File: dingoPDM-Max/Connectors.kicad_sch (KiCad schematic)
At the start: 13 parts, among them J1 RedCubeTerminal, J2 USB_C_Receptacle_USB2.0, J3 RedCubeTerminal, J4 Conn_01x12

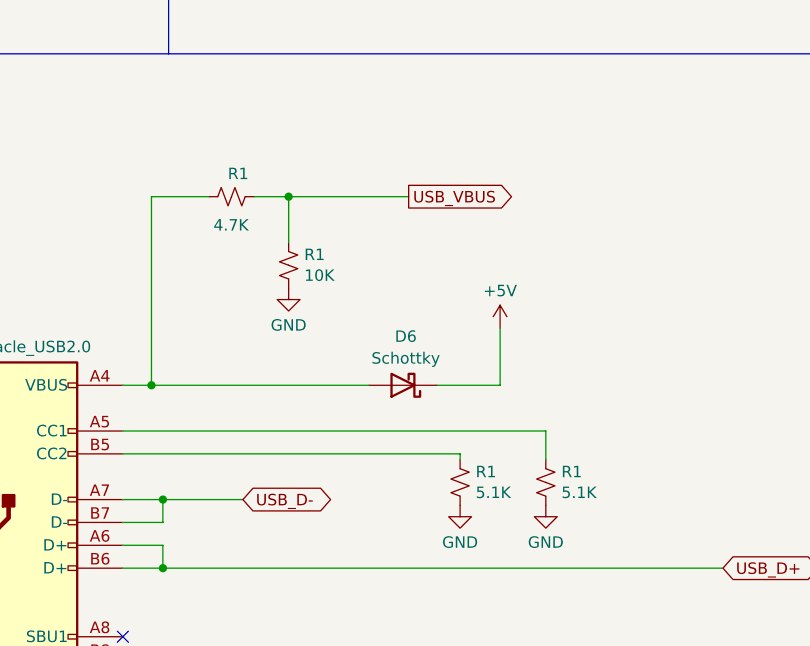
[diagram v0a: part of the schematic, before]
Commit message: Updated to Kicad 8
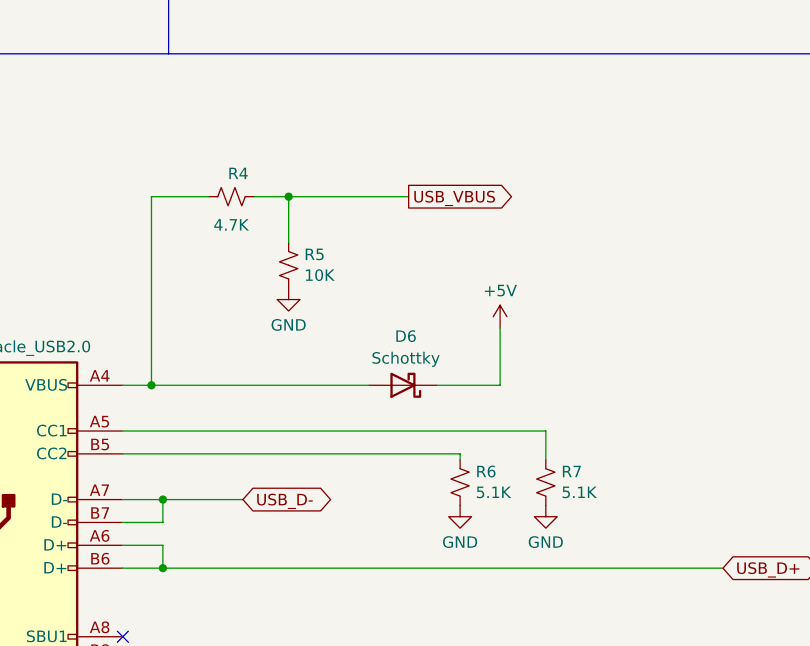
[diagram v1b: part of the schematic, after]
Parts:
- renumbered R1 to R4, R1 to R5, R1 to R6, R1 to R7

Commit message: add dc-dc options and 5v cap
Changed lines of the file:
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@@
 (kicad_sch
-	(version 20231120)
+	(version 20250114)
 	(generator "eeschema")
-	(generator_version "8.0")
+	(generator_version "9.0")
 	(paper "USLetter")
 	(title_block
 		(title "dingoPDM-Max")
-		(date "2024-09-06")
-		(rev "v1.0")
+		(date "2025-06-16")
+		(rev "v1.1")
 		(comment 3 "github.com/corygrant")
 		(comment 4 "Cory Grant")
+	)
+	(text "Deutsch DT"
+		(exclude_from_sim no)
+		(at 167.005 99.695 0)
+		(effects
+			(font
+				(size 1.27 1.27)
+				(thickness 0.254)
+				(bold yes)
+			)
+			(justify right bottom)
+		)
+	)
+	(text "Battery Lug"
+		(exclude_from_sim no)
+		(at 50.165 52.705 0)
+		(effects
+			(font
+				(size 1.27 1.27)
+				(thickness 0.254)
+				(bold yes)
+			)
+			(justify right bottom)
+		)
+	)
+	(text "Mounting Holes"
+		(exclude_from_sim no)
+		(at 50.165 58.42 0)
+		(effects
+			(font
+				(size 1.27 1.27)
+				(thickness 0.254)
+				(bold yes)
+			)
+			(justify right bottom)
+		)
 	)
 	(junction
@@
 			"+fKIESPmzZu3cOFCJycnCwuLXujt2MuAqVCpVCtXrrx161Z6ejq0gOoWMLqEAQMGAxmmoQ6yCwhO"
 			"f2poaCguLoaOkDqdbubMmQsXLgwICODz+biX0sAA+LU2bdoUFxcXHx/v4+PTLaf9Pw2dsqpV3O3n"
-			"AAAAAElFTkSuQmCC"
-		)
-	)
-	(text "Deutsch DT"
-		(exclude_from_sim no)
-		(at 167.005 99.695 0)
-		(effects
-			(font
-				(size 1.27 1.27)
-				(thickness 0.254)
-				(bold yes)
-			)
-			(justify right bottom)
-		)
-	)
-	(text "Battery Lug"
-		(exclude_from_sim no)
-		(at 50.165 52.705 0)
-		(effects
-			(font
-				(size 1.27 1.27)
-				(thickness 0.254)
-				(bold yes)
-			)
-			(justify right bottom)
-		)
-	)
-	(text "Mounting Holes"
-		(exclude_from_sim no)
-		(at 50.165 58.42 0)
-		(effects
-			(font
-				(size 1.27 1.27)
-				(thickness 0.254)
-				(bold yes)
-			)
-			(justify right bottom)
-		)
-	)
+			"AAAAAElFTkSuQmCCAAAAAAAAAAAAAAAAAAAAAAAAAAAAAAAAAAAAAAAAAAAAAAAAAAAAAAAAAAAA"
+			"AAAAAAAAAAAAAAAAAAAAAAAAAAAAAAAAAAAAAAAAAAAAAAAAAAAAAAAAAAAAAAAAAAAAAAAAAAAA"
+			"AAAAAAAAAAAAAAAAAAAAAAAAAAAAAAAAAAAAAAAAAAAAAAAAAAAAAAAAAAAAAAAAAAAAAAAAAAAA"
+			"AAAAAAAAAAAAAAAAAAAAAAAAAAAAAAAAAAAAAAAAAAAAAAAAAAAAAAAAAAAAAAAAAAAAAAAAAAAA"
+			"AAAAAAAAAAAAAAAAAAAAAAAAAAAAAAAAAAAAAAAAAAAAAAAAAAAAAAAAAAAAAAAAAAAAAAAAAAAA"
+			"AAAAAAAAAAAAAAAAAAAAAAAAAAAAAAAAAAAAAAAAAAAAAAAAAAAAAAAAAAAAAAAAAAAAAAAAAAAA"
+			"AAAAAAAAAAAAAAAAAAAAAAAAAAAAAAAAAAAAAAAAAAAAAAAAAAAAAAAAAAAAAAAAAAAAAAAAAAAA"
+			"AAAAAAAAAAAAAAAAAAAAAAAAAAAAAAAAAAAAAAAAAAAAAAAAAAAAAAAAAAAAAAAAAAAAAAAAAAAA"
+			"AAAAAAAAAAAAAAAAAAAAAAAAAAAAAAAAAAAAAAAAAAAAAAAAAAAAAAAAAAAAAAAAAAAAAAAAAAAA"
+			"AAAAAAAAAAAAAAAAAAAAAAAAAAAAAAAAAAAAAAAAAAAAAAAAAAAAAAAAAAAAAAAAAAAAAAAAAAAA"
+			"AAAAAAAAAAAAAAAAAAAAAAAAAAAAAAAAAAAAAAAAAAAAAAAAAAAAAAAAAAAAAAAAAAAAAAAAAAAA"
+			"AAAAAAAAAAAAAAAAAAAAAAAAAAAAAAAAAAAAAAAAAAAAAAAAAAAAAAAAAAAAAAAAAAAAAAAAAAAA"
+			"AAAAAAAAAAAAAAAAAAAAAAAAAAAAAAAAAAAAAAAAAAAAAAAAAAAAAAAAAAAAAAAAAAAAAAAAAAAA"
+			"AAAAAAAAAAAAAAAAAAAAAAAAAAAAAAAAAAAAAAAAAAAAAAAAAAAAAAAAAAAAAAAAAAAAAAAAAAAA"
+			"AAAAAAAAAAAAAAAAAAAAAAAAAAAAAAAAAAAAAAAAAAAAAAAAAAAAAAAAAAAAAAAAAAAAAAAAAAAA"
+			"AAAAAAAAAAAAAAAAAAAAAAAAAAAAAAAAAAAAAAAAAAAAAAAAAAAAAAAAAAAAAAAAAAAAAAAAAAAA"
+			"AAAAAAAAAAAAAAAAAAAAAAAAAAAAAAAAAAAAAAAAAAAAAAAAAAAAAAAAAAAAAAAAAAAAAAAAAAAA"
+			"AAAAAAAAAAAAAAAAAAAAAAAAAAAAAAAAAAAAAAAAAAAAAAAAAAAAAAAAAAAAAAAAAAAAAAAAAAAA"
+			"AAAAAAAAAAAAAA=="
+		)
+	)

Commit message: fixed bad zone, shifted traces, increase trace widths
update part numbers for ibom
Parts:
- J1, J3: LCSC (none) -> C6828431
- J2: LCSC (none) -> C7095263
- J4: LCSC (none) -> C5341788
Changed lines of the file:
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@@
 	(title_block
 		(title "dingoPDM-Max")
-		(date "2025-06-16")
-		(rev "v1.1")
+		(date "2025-09-29")
+		(rev "v1.2")
 		(comment 3 "github.com/corygrant")
 		(comment 4 "Cory Grant")
@@
 			)
 		)
-		(property "LCSC" ""
+		(property "LCSC" "C6828431"
 			(at 22.86 31.75 0)
 			(effects
@@
 			)
 		)
-		(property "LCSC" ""
+		(property "LCSC" "C5341788"
 			(at 106.68 56.515 0)
 			(effects
@@
 			)
 		)
-		(property "LCSC" ""
+		(property "LCSC" "C6828431"
 			(at 31.75 34.29 0)
 			(effects
@@
 			(at 31.115 153.67 0)
 			(effects
+				(font
+					(size 1.27 1.27)
+				)
+				(hide yes)
+			)
+		)
+		(property "LCSC" "C7095263"
+			(at 31.115 153.67 0)
+			(effects
